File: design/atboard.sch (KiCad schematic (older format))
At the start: 7 parts, among them J1 AVR_SPI, J2 Conn_01x14, J3 Conn_01x14, U1 ATmega328-PU, Y1 8 MHz

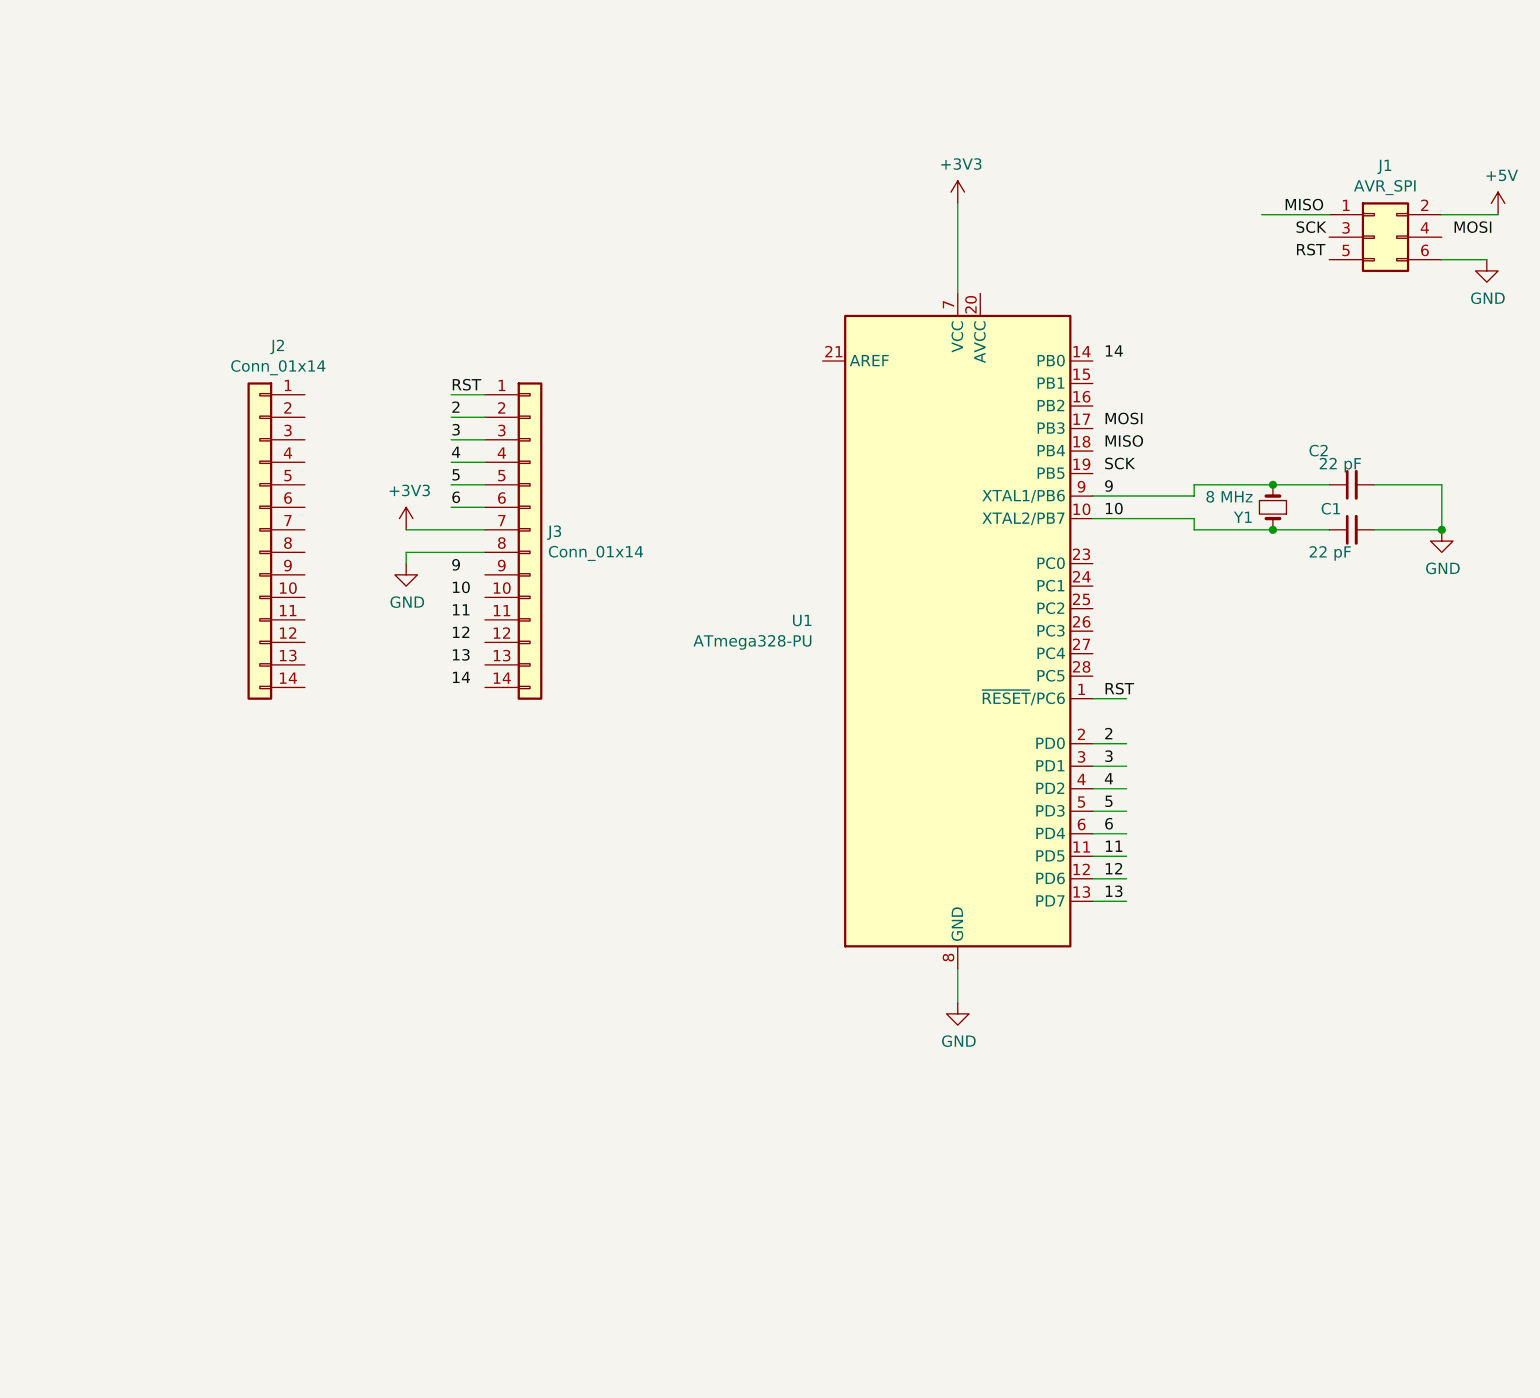
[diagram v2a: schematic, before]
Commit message: added power connector more pins connected to the header
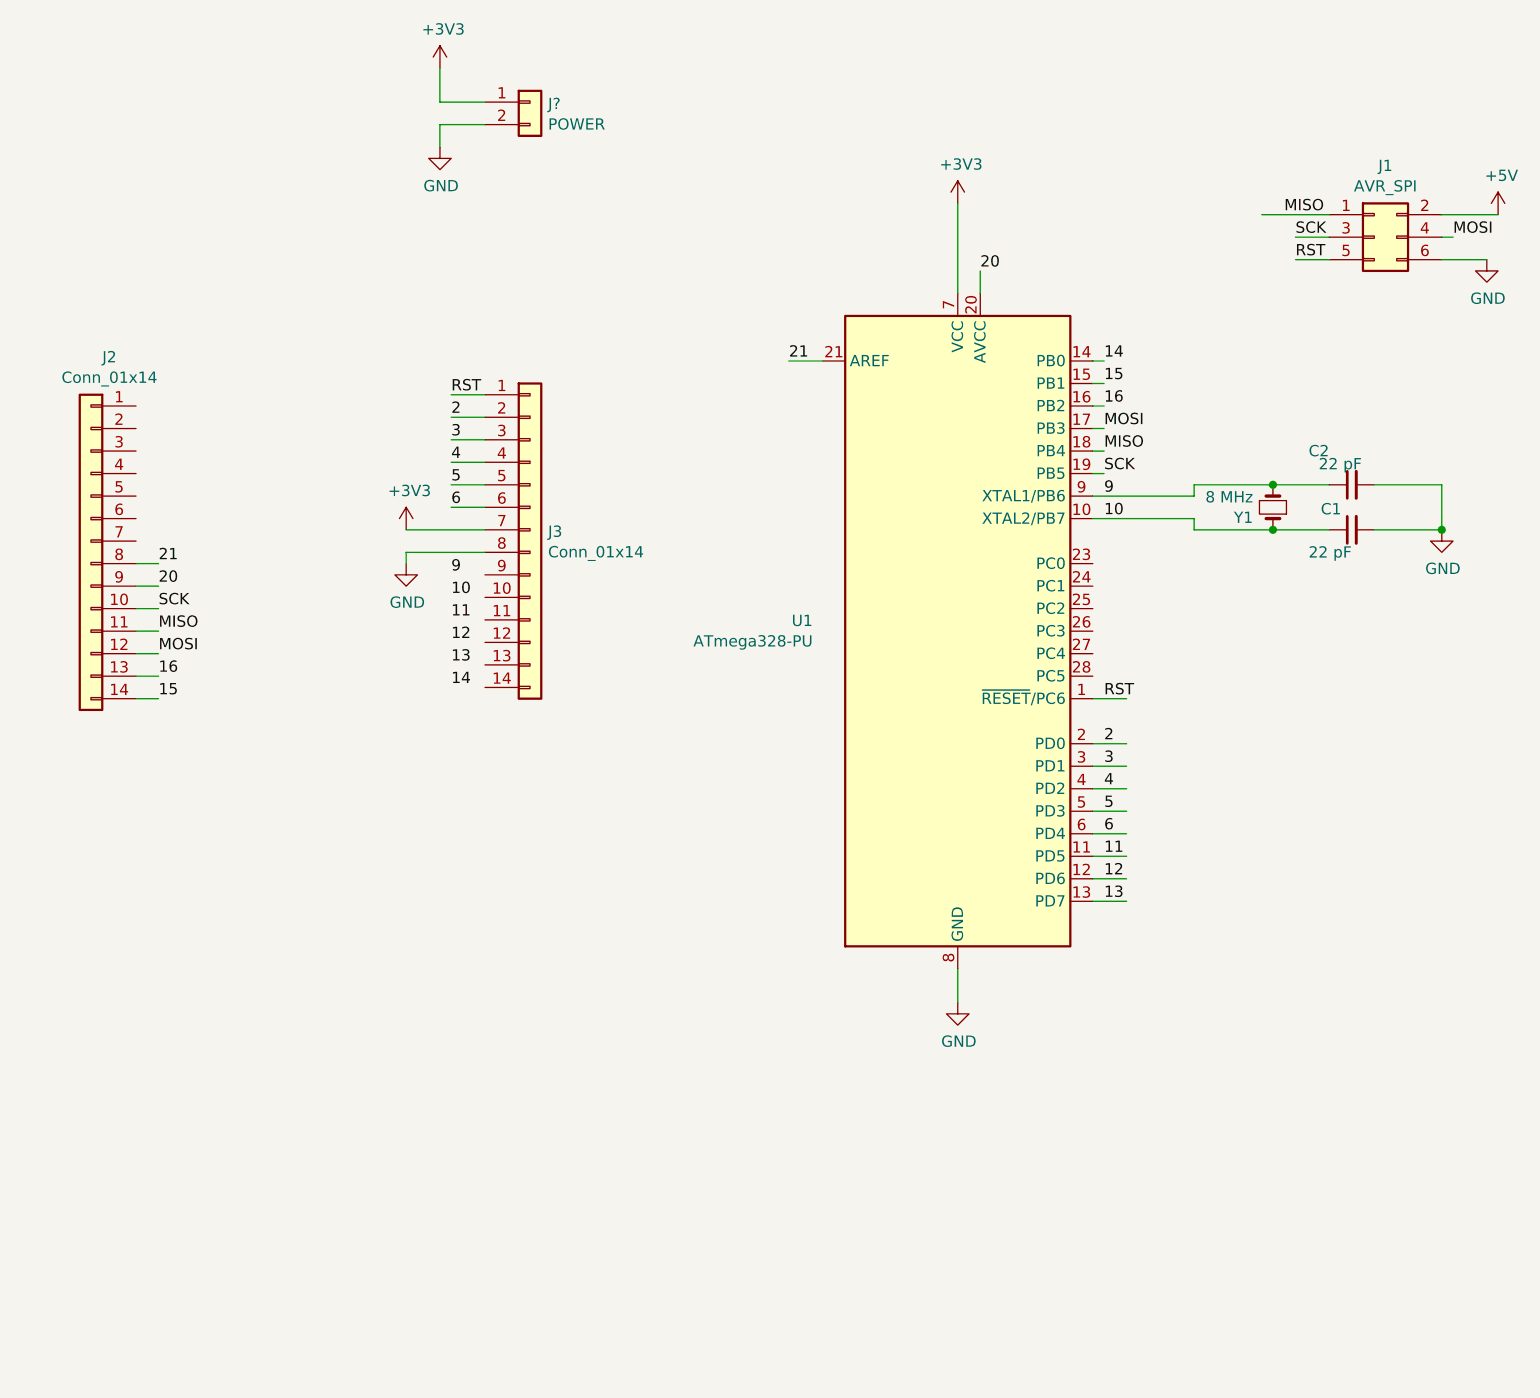
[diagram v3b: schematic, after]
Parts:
- added J?: POWER, Connector_JST:JST_PH_S2B-PH-K_1x02_P2.00mm_Horizontal, symbol Connector_Generic:Conn_01x02
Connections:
- net labels added: 15, 16, 20, 21
- wire segments 34 -> 56
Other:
- moved on the sheet: J2
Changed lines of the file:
@@
 	1    0    0    -1
-$EndComp
-$Comp
-L Connector_Generic:Conn_01x14 J2
-U 1 1 5CC0C46F
-P 3250 3750
-F 0 "J2" H 3168 4567 50  0000 C CNN
-F 1 "Conn_01x14" H 3168 4476 50  0000 C CNN
-F 2 "Connector_PinHeader_2.54mm:PinHeader_1x14_P2.54mm_Vertical" H 3250 3750 50  0001 C CNN
-F 3 "~" H 3250 3750 50  0001 C CNN
-	1    3250 3750
-	-1   0    0    -1
 $EndComp
 Text Label 4100 3150 0    50   ~ 0
@@
 Wire Wire Line
 	6950 4500 7100 4500
+$Comp
+L Connector_Generic:Conn_01x02 J?
+U 1 1 5CBF987B
+P 4450 1850
+F 0 "J?" H 4530 1842 50  0000 L CNN
+F 1 "POWER" H 4530 1751 50  0000 L CNN
+F 2 "Connector_JST:JST_PH_S2B-PH-K_1x02_P2.00mm_Horizontal" H 4450 1850 50  0001 C CNN
+F 3 "~" H 4450 1850 50  0001 C CNN
+	1    4450 1850
+	1    0    0    -1
+$EndComp
+$Comp
+L power:+3V3 #PWR?
+U 1 1 5CBF9E30
+P 4050 1700
+F 0 "#PWR?" H 4050 1550 50  0001 C CNN
+F 1 "+3V3" H 4065 1873 50  0000 C CNN
+F 2 "" H 4050 1700 50  0001 C CNN
+F 3 "" H 4050 1700 50  0001 C CNN
+	1    4050 1700
+	1    0    0    -1
+$EndComp
+$Comp
+L power:GND #PWR?
+U 1 1 5CBFA7FE
+P 4050 2050
+F 0 "#PWR?" H 4050 1800 50  0001 C CNN
+F 1 "GND" H 4055 1877 50  0000 C CNN
+F 2 "" H 4050 2050 50  0001 C CNN
+F 3 "" H 4050 2050 50  0001 C CNN
+	1    4050 2050
+	1    0    0    -1
+$EndComp
+Wire Wire Line
+	4250 1950 4050 1950
+Wire Wire Line
+	4050 1950 4050 2050
+Wire Wire Line
+	4250 1850 4050 1850
+Wire Wire Line
+	4050 1850 4050 1700
+Text Label 7000 3100 0    50   ~ 0
+15
+$Comp
+L Connector_Generic:Conn_01x14 J2
+U 1 1 5CC0C46F
+P 2500 3800
+F 0 "J2" H 2418 4617 50  0000 C CNN
+F 1 "Conn_01x14" H 2418 4526 50  0000 C CNN
+F 2 "Connector_PinHeader_2.54mm:PinHeader_1x14_P2.54mm_Vertical" H 2500 3800 50  0001 C CNN
+F 3 "~" H 2500 3800 50  0001 C CNN
+	1    2500 3800
+	-1   0    0    -1
+$EndComp
+Text Label 2800 4500 0    50   ~ 0
+15
+Text Label 7000 3200 0    50   ~ 0
+16
+Text Label 2800 4400 0    50   ~ 0
+16
+Text Label 2800 4300 0    50   ~ 0
+MOSI
+Text Label 2800 4200 0    50   ~ 0
+MISO
+Text Label 2800 4100 0    50   ~ 0
+SCK
+Text Label 2800 4000 0    50   ~ 0
+20
+Text Label 6450 2600 0    50   ~ 0
+20
+Wire Wire Line
+	2700 4500 2800 4500
+Wire Wire Line
+	2700 4400 2800 4400
+Wire Wire Line
+	2700 4300 2800 4300
+Wire Wire Line
+	2700 4200 2800 4200
+Wire Wire Line
+	2700 4100 2800 4100
+Wire Wire Line
+	2700 4000 2800 4000
+Text Label 5600 3000 0    50   ~ 0
+21
+Text Label 2800 3900 0    50   ~ 0
+21
+Wire Wire Line
+	6450 2700 6450 2600
+Wire Wire Line
+	5750 3000 5600 3000
+Wire Wire Line
+	2700 3900 2800 3900
+Wire Wire Line
+	6950 3500 7000 3500
+Wire Wire Line
+	6950 3400 7000 3400
+Wire Wire Line
+	6950 3300 7000 3300
+Wire Wire Line
+	6950 3200 7000 3200
+Wire Wire Line
+	6950 3100 7000 3100
+Wire Wire Line
+	6950 3000 7000 3000
+Wire Wire Line
+	8000 2450 7850 2450
+Wire Wire Line
+	8000 2550 7850 2550
+Wire Wire Line
+	8500 2450 8550 2450
 $EndSCHEMATC

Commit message: connect the rest
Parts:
- J2: value Conn_01x14 -> RIGHT_CONNECTOR
- J3: value Conn_01x14 -> LEFT_CONNECTOR
- gave numbers to parts that had none: 1
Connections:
- net labels added: 22, 23, 24, 25, 26, 27, 28
- wire segments 56 -> 75
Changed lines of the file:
@@
 P 4450 3750
 F 0 "J3" H 4530 3742 50  0000 L CNN
-F 1 "Conn_01x14" H 4530 3651 50  0000 L CNN
+F 1 "LEFT_CONNECTOR" H 4530 3651 50  0000 L CNN
 F 2 "Connector_PinHeader_2.54mm:PinHeader_1x14_P2.54mm_Vertical" H 4450 3750 50  0001 C CNN
 F 3 "~" H 4450 3750 50  0001 C CNN
@@
 	6950 4500 7100 4500
 $Comp
-L Connector_Generic:Conn_01x02 J?
+L Connector_Generic:Conn_01x02 J4
 U 1 1 5CBF987B
 P 4450 1850
-F 0 "J?" H 4530 1842 50  0000 L CNN
+F 0 "J4" H 4530 1842 50  0000 L CNN
 F 1 "POWER" H 4530 1751 50  0000 L CNN
 F 2 "Connector_JST:JST_PH_S2B-PH-K_1x02_P2.00mm_Horizontal" H 4450 1850 50  0001 C CNN
@@
 $EndComp
 $Comp
-L power:+3V3 #PWR?
+L power:+3V3 #PWR0108
 U 1 1 5CBF9E30
 P 4050 1700
-F 0 "#PWR?" H 4050 1550 50  0001 C CNN
+F 0 "#PWR0108" H 4050 1550 50  0001 C CNN
 F 1 "+3V3" H 4065 1873 50  0000 C CNN
 F 2 "" H 4050 1700 50  0001 C CNN
@@
 $EndComp
 $Comp
-L power:GND #PWR?
+L power:GND #PWR0109
 U 1 1 5CBFA7FE
 P 4050 2050
-F 0 "#PWR?" H 4050 1800 50  0001 C CNN
+F 0 "#PWR0109" H 4050 1800 50  0001 C CNN
 F 1 "GND" H 4055 1877 50  0000 C CNN
 F 2 "" H 4050 2050 50  0001 C CNN
@@
 P 2500 3800
 F 0 "J2" H 2418 4617 50  0000 C CNN
-F 1 "Conn_01x14" H 2418 4526 50  0000 C CNN
+F 1 "RIGHT_CONNECTOR" H 2418 4526 50  0000 C CNN
 F 2 "Connector_PinHeader_2.54mm:PinHeader_1x14_P2.54mm_Vertical" H 2500 3800 50  0001 C CNN
 F 3 "~" H 2500 3800 50  0001 C CNN
@@
 Text Label 2800 4000 0    50   ~ 0
 20
-Text Label 6450 2600 0    50   ~ 0
+Text Label 6450 2500 0    50   ~ 0
 20
 Wire Wire Line
@@
 21
 Wire Wire Line
-	6450 2700 6450 2600
+	6450 2700 6450 2500
 Wire Wire Line
 	5750 3000 5600 3000
@@
 Wire Wire Line
 	8500 2450 8550 2450
+$Comp
+L power:GND #PWR0110
+U 1 1 5CC0EF9F
+P 3100 3800
+F 0 "#PWR0110" H 3100 3550 50  0001 C CNN
+F 1 "GND" H 3105 3627 50  0000 C CNN
+F 2 "" H 3100 3800 50  0001 C CNN
+F 3 "" H 3100 3800 50  0001 C CNN
+	1    3100 3800
+	1    0    0    -1
+$EndComp
+Wire Wire Line
+	3100 3800 2700 3800
+Text Label 3100 3800 0    50   ~ 0
+22
+Text Label 2800 3700 0    50   ~ 0
+23
+Text Label 7050 3900 0    50   ~ 0
+23
+Text Label 2800 3600 0    50   ~ 0
+24
+Text Label 7050 4000 0    50   ~ 0
+24
+Text Label 7050 4100 0    50   ~ 0
+25
+Text Label 2800 3500 0    50   ~ 0
+25
+Text Label 2800 3400 0    50   ~ 0
+26
+Text Label 7050 4200 0    50   ~ 0
+26
+Text Label 7050 4300 0    50   ~ 0
+27
+Text Label 2800 3300 0    50   ~ 0
+27
+Text Label 2800 3200 0    50   ~ 0
+28
+Text Label 7050 4400 0    50   ~ 0
+28
+Wire Wire Line
+	2700 3200 2800 3200
+Wire Wire Line
+	2700 3300 2800 3300
+Wire Wire Line
+	2700 3400 2800 3400
+Wire Wire Line
+	2700 3500 2800 3500
+Wire Wire Line
+	2700 3600 2800 3600
+Wire Wire Line
+	2700 3700 2800 3700
+Wire Wire Line
+	6950 3900 7050 3900
+Wire Wire Line
+	6950 4000 7050 4000
+Wire Wire Line
+	6950 4100 7050 4100
+Wire Wire Line
+	6950 4200 7050 4200
+Wire Wire Line
+	6950 4300 7050 4300
+Wire Wire Line
+	6950 4400 7050 4400
+Wire Wire Line
+	4250 3950 4100 3950
+Wire Wire Line
+	4250 4050 4100 4050
+Wire Wire Line
+	4250 4150 4100 4150
+Wire Wire Line
+	4250 4250 4100 4250
+Wire Wire Line
+	4250 4350 4100 4350
+Wire Wire Line
+	4250 4450 4100 4450
 $EndSCHEMATC
